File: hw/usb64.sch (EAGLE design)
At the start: 22 parts

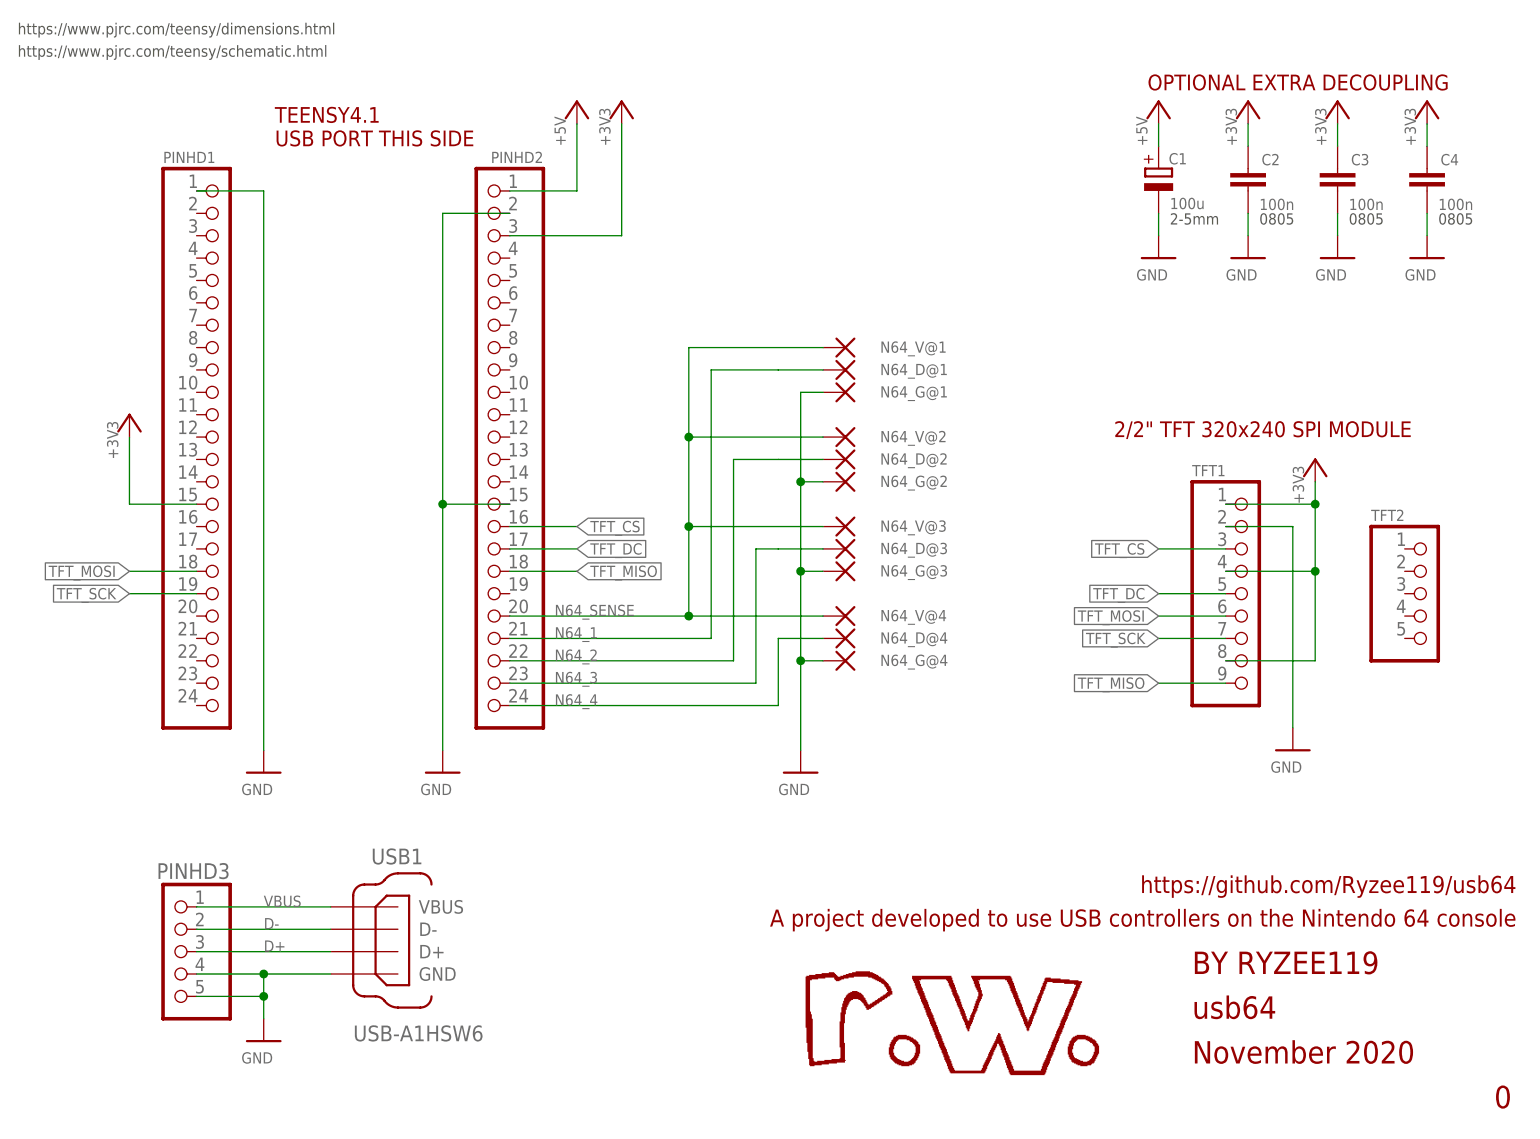
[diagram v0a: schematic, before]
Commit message: hw: Add 100pF filtering capacitors
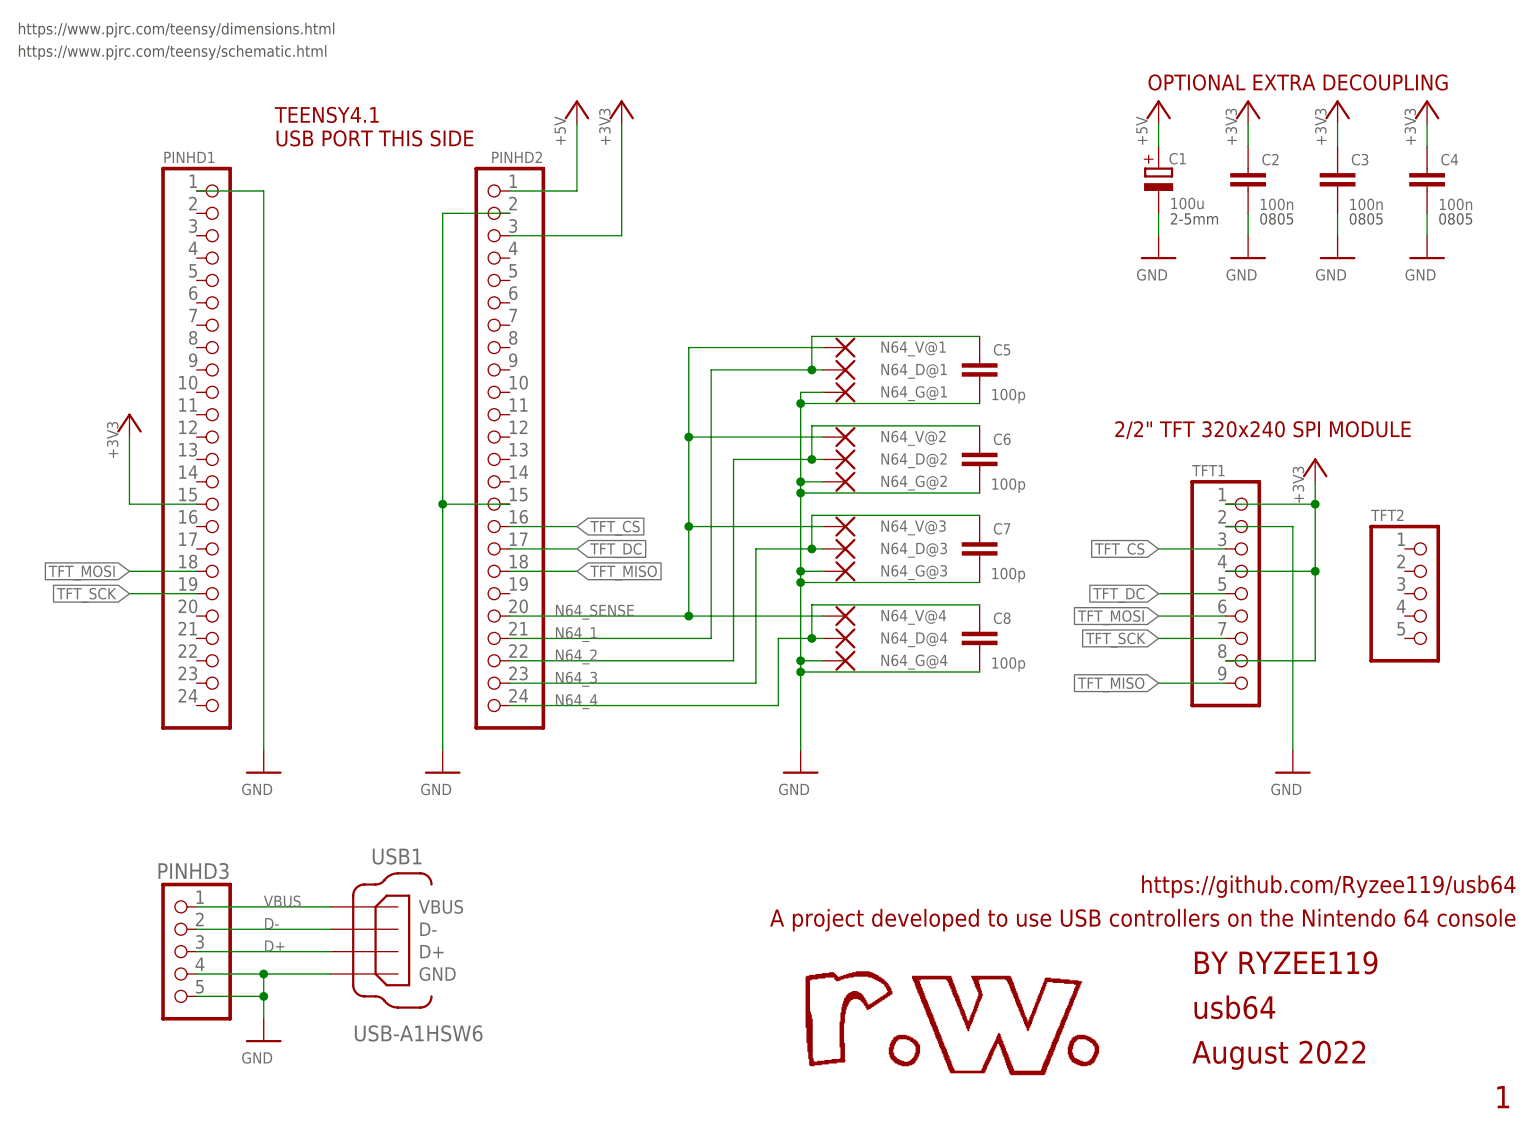
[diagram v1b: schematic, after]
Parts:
- added C5, C6, C7, C8: 100p, rcl:C-EUC0805K
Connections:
- net GND: now also C5.2, C6.2, C7.2, C8.2
- net N64_1: now also C5.1
- net N64_2: now also C6.1
- net N64_3: now also C7.1
- net N64_4: now also C8.1
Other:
- note added: "1"
- note added: "August 2022"
- note removed: "0"
- note removed: "November 2020"
